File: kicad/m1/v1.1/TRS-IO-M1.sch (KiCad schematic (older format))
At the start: 26 parts, among them J1 Conn_02x20_Odd_Even, Q1 2N7000, Q2 2N7000, SW1 SW_Push, U1 HiLetgo-ESP-32S, U2 AS6C62256-PDIP, U3 MCP23S17_SP, U4 74LVC245, U5 74LVC245, U6 74LVC245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

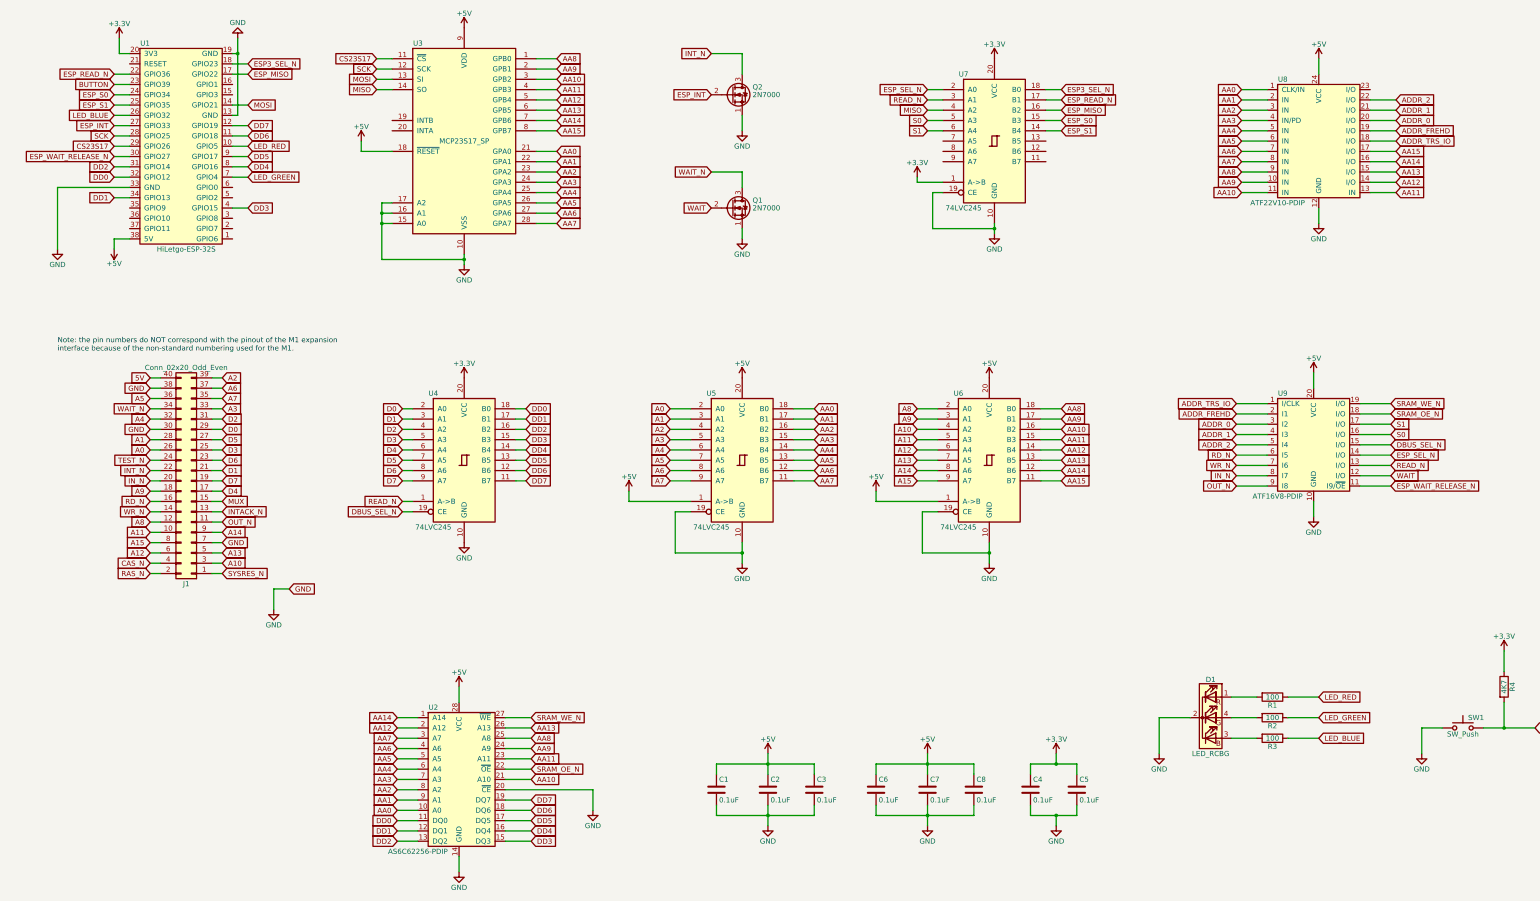
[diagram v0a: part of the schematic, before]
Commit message: Updates for TRS-IO-M1 v1.1
- Move data bus of the SRAM before the buffer
- added J2 for the edge connector
- Removed ADDR_2 and repurposed the connection for RAS*
- Move ESP_SEL_N to GPIO 27
- Move ESP_WAIT_RELEASE_N to GPIO 2
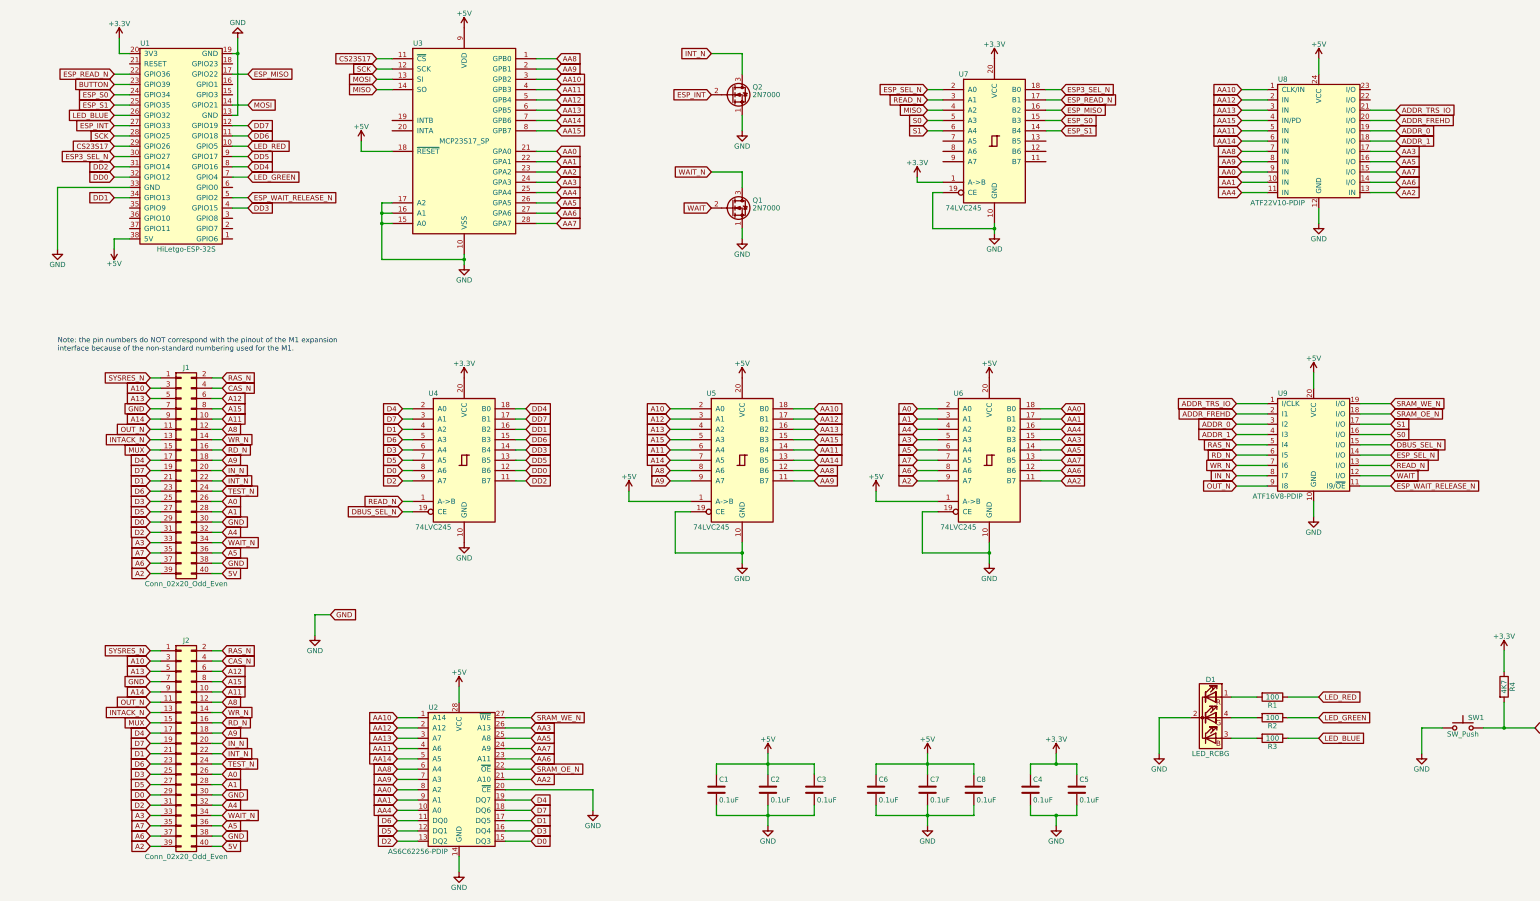
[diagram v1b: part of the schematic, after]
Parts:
- added J2: Conn_02x20_Odd_Even, TRS-IO-M1:TRSEDGE, symbol Connector_Generic:Conn_02x20_Odd_Even
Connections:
- net 5V: now also J2.40 (Pin_40)
- net A0: now also U6.2 (A0), J2.26 (Pin_26); no longer U5.2 (A0)
- net A1: now also U6.3 (A1), J2.28 (Pin_28); no longer U5.3 (A1)
- net A10: now also U5.2 (A0), J2.3 (Pin_3); no longer U6.4 (A2)
- net A11: now also U5.6 (A4), J2.10 (Pin_10); no longer U6.5 (A3)
- net A12: now also U5.3 (A1), J2.6 (Pin_6); no longer U6.6 (A4)
- net A13: now also U5.4 (A2), J2.5 (Pin_5); no longer U6.7 (A5)
- net A14: now also U5.7 (A5), J2.9 (Pin_9); no longer U6.8 (A6)
- net A15: now also U5.5 (A3), J2.8 (Pin_8); no longer U6.9 (A7)
- net A2: now also U6.9 (A7), J2.39 (Pin_39); no longer U5.4 (A2)
- net A3: now also U6.5 (A3), J2.33 (Pin_33); no longer U5.5 (A3)
- net A4: now also U6.4 (A2), J2.32 (Pin_32); no longer U5.6 (A4)
- net A5: now also U6.6 (A4), J2.36 (Pin_36); no longer U5.7 (A5)
- net A6: now also U6.8 (A6), J2.37 (Pin_37); no longer U5.8 (A6)
- net A7: now also U6.7 (A5), J2.35 (Pin_35); no longer U5.9 (A7)
- net A8: now also U5.8 (A6), J2.12 (Pin_12); no longer U6.2 (A0)
- net A9: now also U5.9 (A7), J2.18 (Pin_18); no longer U6.3 (A1)
- net AA0: now also U2.8 (A2), U6.18 (B0), U8.9 (IN); no longer U2.10 (A0), U5.18 (B0), U8.1 (CLK/IN)
- net AA1: now also U6.17 (B1), U8.10 (IN); no longer U5.17 (B1), U8.2 (IN)
- net AA10: now also U2.1 (A14), U5.18 (B0), U8.1 (CLK/IN); no longer U2.21 (A10), U6.16 (B2), U8.11 (IN)
- net AA11: now also U2.4 (A6), U5.14 (B4), U8.5 (IN); no longer U2.23 (A11), U6.15 (B3), U8.13 (IN)
- net AA12: now also U5.17 (B1), U8.2 (IN); no longer U6.14 (B4), U8.14 (I/O)
- net AA13: now also U2.3 (A7), U5.16 (B2), U8.3 (IN); no longer U2.26 (A13), U6.13 (B5), U8.15 (I/O)
- net AA14: now also U2.5 (A5), U5.13 (B5), U8.6 (IN); no longer U2.1 (A14), U6.12 (B6), U8.16 (I/O)
- net AA15: now also U5.15 (B3), U8.4 (IN/PD); no longer U6.11 (B7), U8.17 (I/O)
- net AA2: now also U2.21 (A10), U6.11 (B7), U8.13 (IN); no longer U2.8 (A2), U5.16 (B2), U8.3 (IN)
- net AA3: now also U2.26 (A13), U6.15 (B3), U8.17 (I/O); no longer U2.7 (A3), U5.15 (B3), U8.4 (IN/PD)
- net AA4: now also U2.10 (A0), U6.16 (B2), U8.11 (IN); no longer U2.6 (A4), U5.14 (B4), U8.5 (IN)
- net AA5: now also U2.25 (A8), U6.14 (B4), U8.16 (I/O); no longer U2.5 (A5), U5.13 (B5), U8.6 (IN)
- net AA6: now also U2.23 (A11), U6.12 (B6), U8.14 (I/O); no longer U2.4 (A6), U5.12 (B6), U8.7 (IN)
- net AA7: now also U2.24 (A9), U6.13 (B5), U8.15 (I/O); no longer U2.3 (A7), U5.11 (B7), U8.8 (IN)
- net AA8: now also U2.6 (A4), U5.12 (B6), U8.7 (IN); no longer U2.25 (A8), U6.18 (B0), U8.9 (IN)
- net AA9: now also U2.7 (A3), U5.11 (B7), U8.8 (IN); no longer U2.24 (A9), U6.17 (B1), U8.10 (IN)
- net ADDR_0: now also U8.19 (I/O); no longer U8.20 (I/O)
- net ADDR_1: now also U8.18 (I/O); no longer U8.21 (I/O)
- net ADDR_FREHD: now also U8.20 (I/O); no longer U8.19 (I/O)
- net ADDR_TRS_IO: now also U8.21 (I/O); no longer U8.18 (I/O)
- net CAS_N: now also J2.4 (Pin_4)
- net D0: now also U2.15 (DQ3), U4.8 (A6), J2.29 (Pin_29); no longer U4.2 (A0)
- net D1: now also U2.17 (DQ5), U4.4 (A2), J2.21 (Pin_21); no longer U4.3 (A1)
- net D2: now also U2.13 (DQ2), U4.9 (A7), J2.31 (Pin_31); no longer U4.4 (A2)
- net D3: now also U2.16 (DQ4), U4.6 (A4), J2.25 (Pin_25); no longer U4.5 (A3)
- net D4: now also U2.19 (DQ7), U4.2 (A0), J2.17 (Pin_17); no longer U4.6 (A4)
- net D5: now also U2.12 (DQ1), J2.27 (Pin_27)
- net D6: now also U2.11 (DQ0), U4.5 (A3), J2.23 (Pin_23); no longer U4.8 (A6)
- net D7: now also U2.18 (DQ6), U4.3 (A1), J2.19 (Pin_19); no longer U4.9 (A7)
- net DD0: now also U4.12 (B6); no longer U2.11 (DQ0), U4.18 (B0)
- net DD1: now also U4.16 (B2); no longer U2.12 (DQ1), U4.17 (B1)
- net DD2: now also U4.11 (B7); no longer U2.13 (DQ2), U4.16 (B2)
- net DD3: now also U4.14 (B4); no longer U2.15 (DQ3), U4.15 (B3)
- net DD4: now also U4.18 (B0); no longer U2.16 (DQ4), U4.14 (B4)
- net DD5: no longer U2.17 (DQ5)
- net DD6: now also U4.15 (B3); no longer U2.18 (DQ6), U4.12 (B6)
- net DD7: now also U4.17 (B1); no longer U2.19 (DQ7), U4.11 (B7)
- net ESP3_SEL_N: now also U1.30 (GPIO27); no longer U1.18 (GPIO23)
- net ESP_WAIT_RELEASE_N: now also U1.5 (GPIO2); no longer U1.30 (GPIO27)
- net GND: now also J2.30 (Pin_30), J2.38 (Pin_38), J2.7 (Pin_7)
- net INTACK_N: now also J2.13 (Pin_13)
- net INT_N: now also J2.22 (Pin_22)
- net IN_N: now also J2.20 (Pin_20)
- net MUX: now also J2.15 (Pin_15)
- net OUT_N: now also J2.11 (Pin_11)
- net RAS_N: now also U9.5 (I4), J2.2 (Pin_2)
- net RD_N: now also J2.16 (Pin_16)
- net SYSRES_N: now also J2.1 (Pin_1)
- net TEST_N: now also J2.24 (Pin_24)
- net WAIT_N: now also J2.34 (Pin_34)
- net WR_N: now also J2.14 (Pin_14)
- net ADDR_2: no longer names the net of U8.22 (I/O)
- net ADDR_2: no longer U9.5 (I4)
